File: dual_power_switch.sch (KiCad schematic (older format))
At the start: 1 part, among them U3 ITS5215L

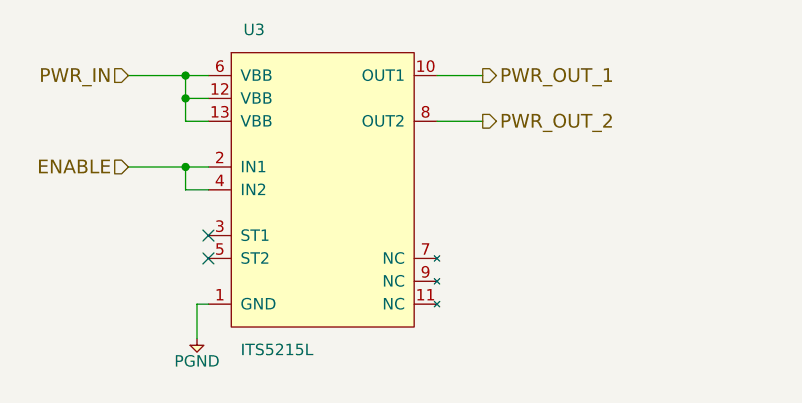
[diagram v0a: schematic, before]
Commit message: add LEDs to indicate switch condition; fix hierarchical sheet issues
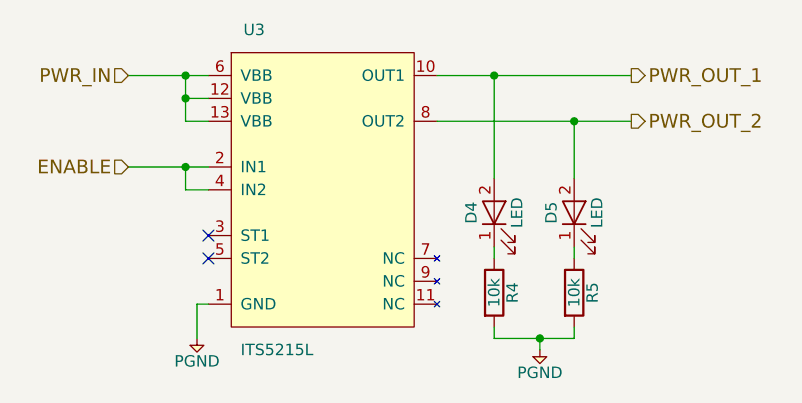
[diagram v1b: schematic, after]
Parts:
- added D4, D5: LED, symbol LED
- added R4, R5: 10k, symbol R
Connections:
- net PGND: now also R4.2, R5.2
- net PWR_OUT_1: now also D4.2 (A)
- net PWR_OUT_2: now also D5.2 (A)
- new net: D4.1 (K), R4.1
- new net: D5.1 (K), R5.1
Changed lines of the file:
@@
+	1    0    0    -1
+$EndComp
+NoConn ~ 5550 4000
+NoConn ~ 5550 4100
+Text HLabel 5200 3300 0    60   Input ~ 0
+PWR_IN
+Text HLabel 5200 3700 0    60   Input ~ 0
+ENABLE
+Text HLabel 7400 3300 2    60   Output ~ 0
+PWR_OUT_1
+Text HLabel 7400 3500 2    60   Output ~ 0
+PWR_OUT_2
+$Comp
+L PGND #PWR013
+U 1 1 5962B650
+P 5500 4450
+F 0 "#PWR013" H 5370 4490 50  0001 L CNN
+F 1 "PGND" H 5500 4350 50  0000 C CNN
+F 2 "" H 5500 4450 60  0001 C CNN
+F 3 "" H 5500 4450 60  0001 C CNN
+	1    5500 4450
+	1    0    0    -1
+$EndComp
+$Comp
+L LED D4
+U 1 1 596A4D7C
+P 6800 3900
+F 0 "D4" H 6800 4000 50  0000 C CNN
+F 1 "LED" H 6800 3800 50  0000 C CNN
+F 2 "" H 6800 3900 50  0001 C CNN
+F 3 "" H 6800 3900 50  0001 C CNN
+	1    6800 3900
+	0    -1   -1   0
+$EndComp
+$Comp
+L LED D5
+U 1 1 596A4DFA
+P 7150 3900
+F 0 "D5" H 7150 4000 50  0000 C CNN
+F 1 "LED" H 7150 3800 50  0000 C CNN
+F 2 "" H 7150 3900 50  0001 C CNN
+F 3 "" H 7150 3900 50  0001 C CNN
+	1    7150 3900
+	0    -1   -1   0
+$EndComp
+$Comp
+L R R4
+U 1 1 596A4F24
+P 6800 4250
+F 0 "R4" V 6880 4250 50  0000 C CNN
+F 1 "10k" V 6800 4250 50  0000 C CNN
+F 2 "" V 6730 4250 50  0001 C CNN
+F 3 "" H 6800 4250 50  0001 C CNN
+	1    6800 4250
+	1    0    0    -1
+$EndComp
+$Comp
+L R R5
+U 1 1 596A4F99
+P 7150 4250
+F 0 "R5" V 7230 4250 50  0000 C CNN
+F 1 "10k" V 7150 4250 50  0000 C CNN
+F 2 "" V 7080 4250 50  0001 C CNN
+F 3 "" H 7150 4250 50  0001 C CNN
+	1    7150 4250
 	1    0    0    -1
 $EndComp
 Wire Wire Line
-	5550 3500 5450 3500
+	5450 3500 5550 3500
 Wire Wire Line
-	5450 3500 5450 3300
+	5450 3300 5450 3500
 Wire Wire Line
 	5200 3300 5550 3300
@@
 Wire Wire Line
 	5550 3800 5450 3800
-NoConn ~ 5550 4000
-NoConn ~ 5550 4100
 Wire Wire Line
 	5550 4300 5500 4300
@@
 	5500 4300 5500 4450
 Wire Wire Line
-	6550 3300 6750 3300
-Wire Wire Line
-	6550 3500 6750 3500
-Text HLabel 5200 3300 0    60   Input ~ 0
-PWR_IN
-Text HLabel 5200 3700 0    60   Input ~ 0
-ENABLE
+	6550 3500 7400 3500
 Wire Wire Line
 	5450 3800 5450 3700
 Connection ~ 5450 3700
-Text HLabel 6750 3300 2    60   Output ~ 0
-PWR_OUT_1
-Text HLabel 6750 3500 2    60   Output ~ 0
-PWR_OUT_2
+Wire Wire Line
+	6550 3300 7400 3300
+Wire Wire Line
+	6800 3750 6800 3300
+Connection ~ 6800 3300
+Wire Wire Line
+	7150 3750 7150 3500
+Connection ~ 7150 3500
+Wire Wire Line
+	6800 4100 6800 4050
+Wire Wire Line
+	7150 4100 7150 4050
 $Comp
-L PGND #PWR13
-U 1 1 5962B650
-P 5500 4450
-F 0 "#PWR13" H 5370 4490 50  0001 L CNN
-F 1 "PGND" H 5500 4350 50  0000 C CNN
-F 2 "" H 5500 4450 60  0001 C CNN
-F 3 "" H 5500 4450 60  0001 C CNN
-	1    5500 4450
+L PGND #PWR014
+U 1 1 596A57A9
+P 7000 4500
+F 0 "#PWR014" H 6870 4540 50  0001 L CNN
+F 1 "PGND" H 7000 4400 50  0000 C CNN
+F 2 "" H 7000 4500 60  0001 C CNN
+F 3 "" H 7000 4500 60  0001 C CNN
+	1    7000 4500
 	1    0    0    -1
 $EndComp
+Wire Wire Line
+	6800 4400 6800 4450
+Wire Wire Line
+	6800 4450 7150 4450
+Wire Wire Line
+	7150 4450 7150 4400
+Wire Wire Line
+	7000 4500 7000 4450
+Connection ~ 7000 4450
 $EndSCHEMATC

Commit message: assign footprints to components
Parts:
- D4, D5: footprint (none) -> LEDs:LED_0805
- R4, R5: footprint (none) -> Resistors_SMD:R_0603
- U3: footprint (none) -> pdb:DSO-12-9
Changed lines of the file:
@@
 F 0 "U3" H 5750 4500 50  0000 C CNN
 F 1 "ITS5215L" H 5850 3100 50  0000 C CNN
-F 2 "" H 7150 2800 50  0001 C CNN
+F 2 "pdb:DSO-12-9" H 7150 2800 50  0001 C CNN
 F 3 "" H 7150 2800 50  0001 C CNN
 	1    6050 3800
@@
 F 0 "D4" H 6800 4000 50  0000 C CNN
 F 1 "LED" H 6800 3800 50  0000 C CNN
-F 2 "" H 6800 3900 50  0001 C CNN
+F 2 "LEDs:LED_0805" H 6800 3900 50  0001 C CNN
 F 3 "" H 6800 3900 50  0001 C CNN
 	1    6800 3900
@@
 F 0 "D5" H 7150 4000 50  0000 C CNN
 F 1 "LED" H 7150 3800 50  0000 C CNN
-F 2 "" H 7150 3900 50  0001 C CNN
+F 2 "LEDs:LED_0805" H 7150 3900 50  0001 C CNN
 F 3 "" H 7150 3900 50  0001 C CNN
 	1    7150 3900
@@
 F 0 "R4" V 6880 4250 50  0000 C CNN
 F 1 "10k" V 6800 4250 50  0000 C CNN
-F 2 "" V 6730 4250 50  0001 C CNN
+F 2 "Resistors_SMD:R_0603" V 6730 4250 50  0001 C CNN
 F 3 "" H 6800 4250 50  0001 C CNN
 	1    6800 4250
@@
 F 0 "R5" V 7230 4250 50  0000 C CNN
 F 1 "10k" V 7150 4250 50  0000 C CNN
-F 2 "" V 7080 4250 50  0001 C CNN
+F 2 "Resistors_SMD:R_0603" V 7080 4250 50  0001 C CNN
 F 3 "" H 7150 4250 50  0001 C CNN
 	1    7150 4250
